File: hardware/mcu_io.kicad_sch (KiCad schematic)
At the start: 23 parts, among them J4 SWD, U10 74HC595D, U11 74HC595D, U12 74HC595D, U13 74HC595D, U6 74HC165D, U7 74HC165D, U8 74HC165D, U9 74HC165D

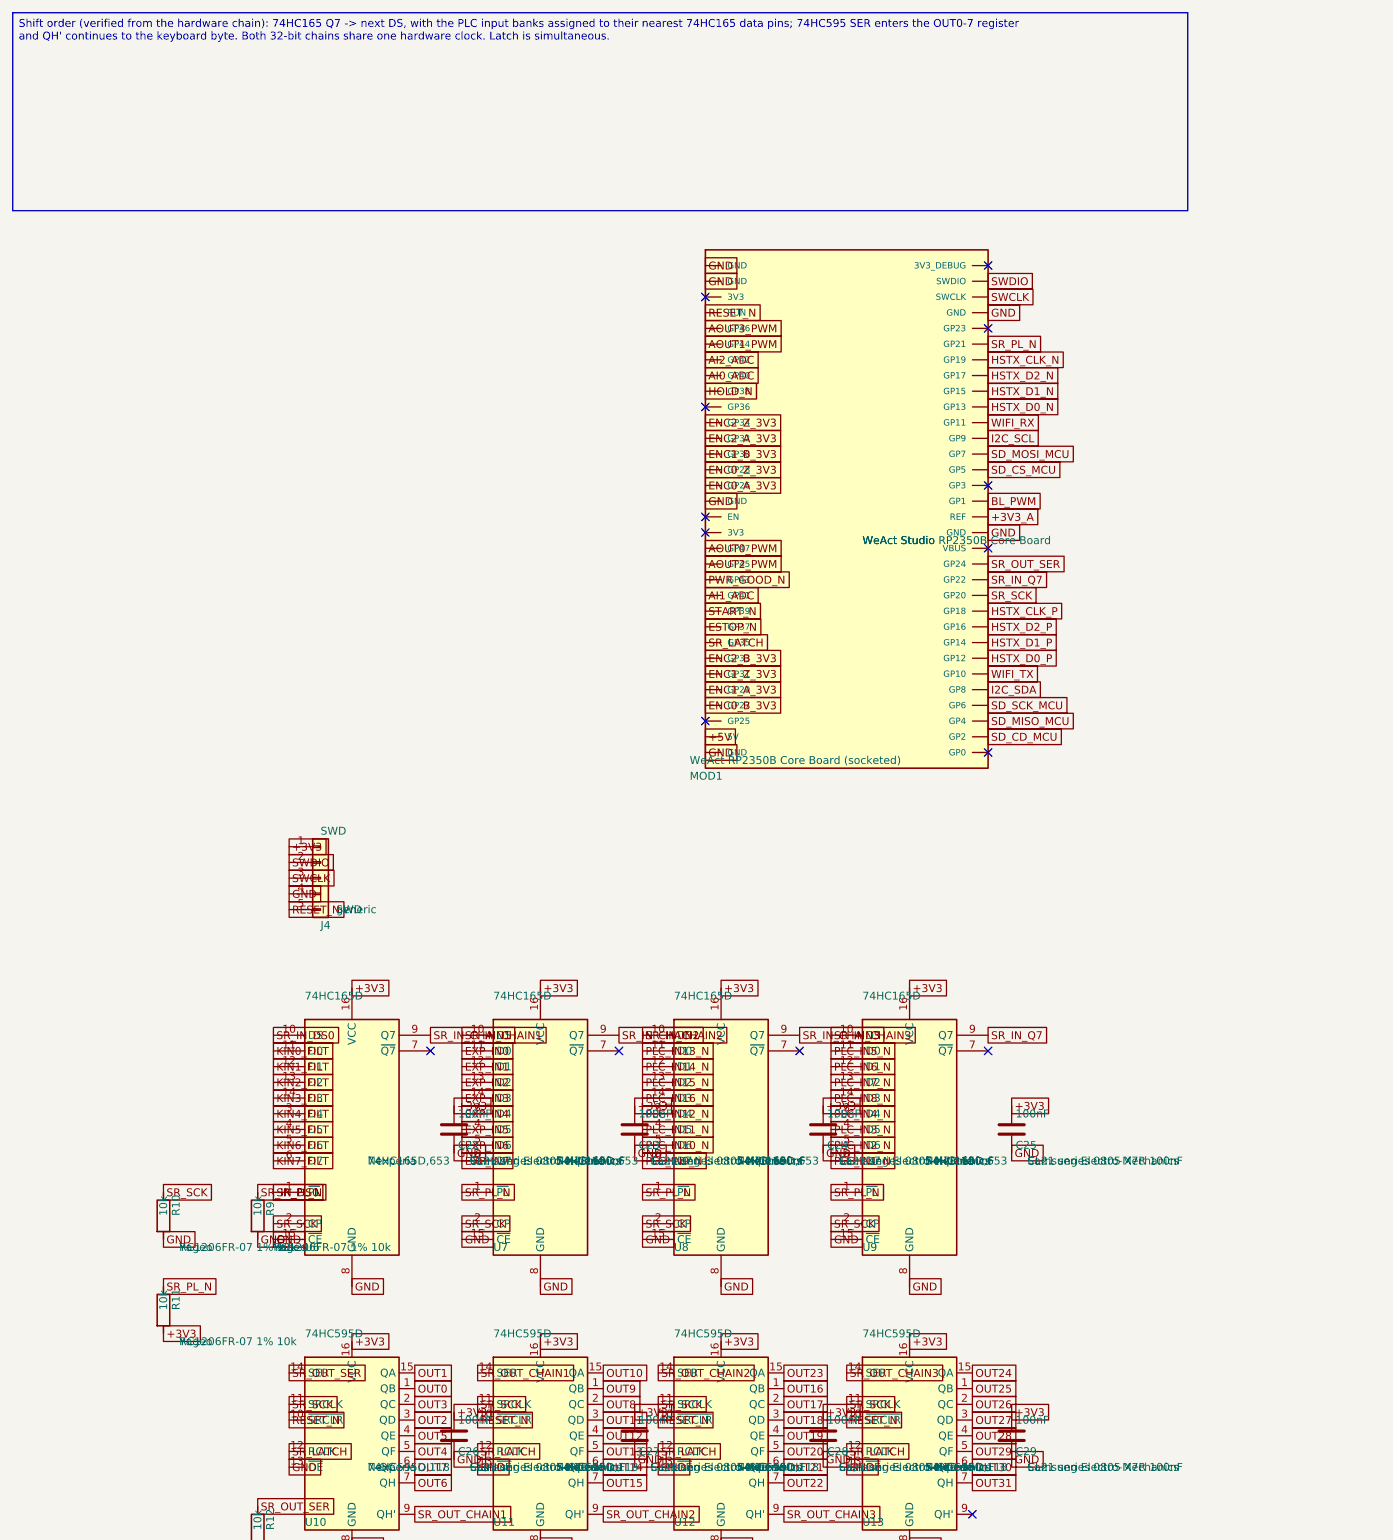
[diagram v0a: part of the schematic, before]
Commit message: Update RP2350B PCB, pinout and fabrication rules
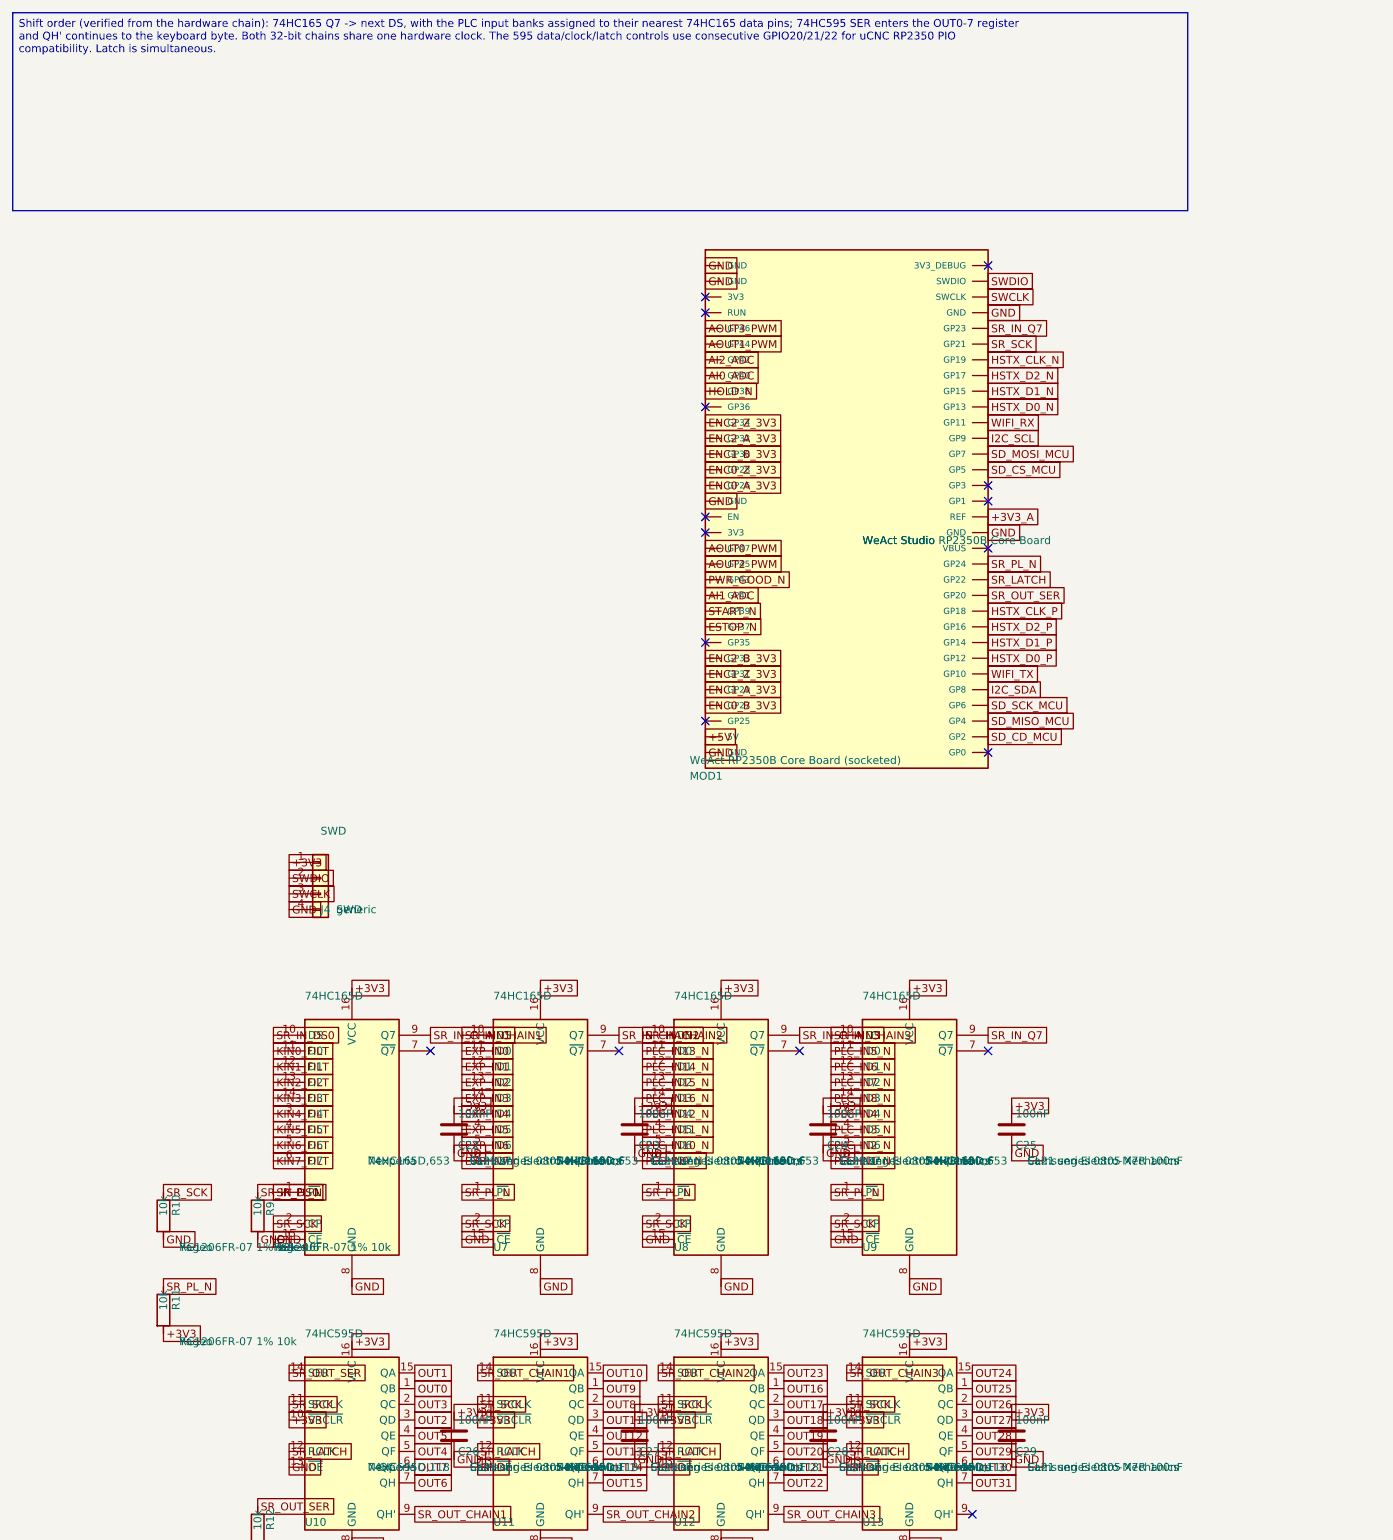
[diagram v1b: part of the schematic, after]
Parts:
- removed J4: SWD, Connector_PinHeader_2.54mm:PinHeader_1x05_P2.54mm_Vertical, symbol Connector_Generic:Conn_01x05
- added J4: SWD, Connector_PinHeader_2.54mm:PinHeader_1x04_P2.54mm_Vertical, symbol Connector_Generic:Conn_01x04
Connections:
- net +3V3: now also U10.10 (~{SRCLR}), U11.10 (~{SRCLR}), U12.10 (~{SRCLR}), U13.10 (~{SRCLR}), J4.1 (Pin_1)
- net GND: now also J4.4 (Pin_4)
- net SR_IN_Q7: now also MOD1.60 (GP23); no longer MOD1.44 (GP22)
- net SR_LATCH: now also MOD1.44 (GP22); no longer MOD1.25 (GP35)
- net SR_OUT_SER: now also MOD1.43 (GP20); no longer MOD1.45 (GP24)
- net SR_PL_N: now also MOD1.45 (GP24); no longer MOD1.59 (GP21)
- net SR_SCK: now also MOD1.59 (GP21); no longer MOD1.43 (GP20)
- net SWCLK: now also J4.3 (Pin_3)
- net SWDIO: now also J4.2 (Pin_2)
- net BL_PWM: no longer names the net of MOD1.49 (GP1)
- removed net RESET_N: MOD1.4 (RUN), U10.10 (~{SRCLR}), U11.10 (~{SRCLR}), U12.10 (~{SRCLR}), U13.10 (~{SRCLR})
- no-connect marks 15 -> 17
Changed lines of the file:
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@@
 		(instances
 			(project "MCU, shift chains and safety"
-				(path "/25c780e5-c6e9-4559-969f-d8c3f97e8b52"
+				(path "/75c4b43e-1edc-48d3-8217-1213416fdce8"
 					(reference "MOD1")
 					(unit 1)
@@
 	)
 	(symbol
-		(lib_id "Connector_Generic:Conn_01x05")
+		(lib_id "Connector_Generic:Conn_01x04")
 		(at 64.77 154.94 0)
 		(unit 1)
@@
 		(fields_autoplaced no)
 		(property "Reference" "J4"
-			(at 64.77 162.56 0.0000)
+			(at 64.77 160.02 0.0000)
 			(effects
 				(font
@@
 			)
 		)
-		(property "Footprint" "Connector_PinHeader_2.54mm:PinHeader_1x05_P2.54mm_Vertical"
+		(property "Footprint" "Connector_PinHeader_2.54mm:PinHeader_1x04_P2.54mm_Vertical"
 			(at 64.77 154.94 0.0000)
 			(effects
@@
 		(pin "4"
 		)
-		(pin "5"
-		)
 		(instances
 			(project "MCU, shift chains and safety"
-				(path "/25c780e5-c6e9-4559-969f-d8c3f97e8b52"
+				(path "/75c4b43e-1edc-48d3-8217-1213416fdce8"
 					(reference "J4")
 					(unit 1)
@@
 		(instances
 			(project "MCU, shift chains and safety"
-				(path "/25c780e5-c6e9-4559-969f-d8c3f97e8b52"
+				(path "/75c4b43e-1edc-48d3-8217-1213416fdce8"
 					(reference "U6")
 					(unit 1)
@@
 		(instances
 			(project "MCU, shift chains and safety"
-				(path "/25c780e5-c6e9-4559-969f-d8c3f97e8b52"
+				(path "/75c4b43e-1edc-48d3-8217-1213416fdce8"
 					(reference "C22")
 					(unit 1)
@@
 		(instances
 			(project "MCU, shift chains and safety"
-				(path "/25c780e5-c6e9-4559-969f-d8c3f97e8b52"
+				(path "/75c4b43e-1edc-48d3-8217-1213416fdce8"
 					(reference "U7")
 					(unit 1)
@@
 		(instances
 			(project "MCU, shift chains and safety"
-				(path "/25c780e5-c6e9-4559-969f-d8c3f97e8b52"
+				(path "/75c4b43e-1edc-48d3-8217-1213416fdce8"
 					(reference "C23")
 					(unit 1)
@@
 		(instances
 			(project "MCU, shift chains and safety"
-				(path "/25c780e5-c6e9-4559-969f-d8c3f97e8b52"
+				(path "/75c4b43e-1edc-48d3-8217-1213416fdce8"
 					(reference "U8")
 					(unit 1)
@@
 		(instances
 			(project "MCU, shift chains and safety"
-				(path "/25c780e5-c6e9-4559-969f-d8c3f97e8b52"
+				(path "/75c4b43e-1edc-48d3-8217-1213416fdce8"
 					(reference "C24")
 					(unit 1)
@@
 		(instances
 			(project "MCU, shift chains and safety"
-				(path "/25c780e5-c6e9-4559-969f-d8c3f97e8b52"
+				(path "/75c4b43e-1edc-48d3-8217-1213416fdce8"
 					(reference "U9")
 					(unit 1)
@@
 		(instances
 			(project "MCU, shift chains and safety"
-				(path "/25c780e5-c6e9-4559-969f-d8c3f97e8b52"
+				(path "/75c4b43e-1edc-48d3-8217-1213416fdce8"
 					(reference "C25")
 					(unit 1)
@@
 		(instances
 			(project "MCU, shift chains and safety"
-				(path "/25c780e5-c6e9-4559-969f-d8c3f97e8b52"
+				(path "/75c4b43e-1edc-48d3-8217-1213416fdce8"
 					(reference "R9")
 					(unit 1)
@@
 		(instances
 			(project "MCU, shift chains and safety"
-				(path "/25c780e5-c6e9-4559-969f-d8c3f97e8b52"
+				(path "/75c4b43e-1edc-48d3-8217-1213416fdce8"
 					(reference "R10")
 					(unit 1)
@@
 		(instances
 			(project "MCU, shift chains and safety"
-				(path "/25c780e5-c6e9-4559-969f-d8c3f97e8b52"
+				(path "/75c4b43e-1edc-48d3-8217-1213416fdce8"
 					(reference "R11")
 					(unit 1)
@@
 		(instances
 			(project "MCU, shift chains and safety"
-				(path "/25c780e5-c6e9-4559-969f-d8c3f97e8b52"
+				(path "/75c4b43e-1edc-48d3-8217-1213416fdce8"
 					(reference "U10")
 					(unit 1)
@@
 		(instances
 			(project "MCU, shift chains and safety"
-				(path "/25c780e5-c6e9-4559-969f-d8c3f97e8b52"
+				(path "/75c4b43e-1edc-48d3-8217-1213416fdce8"
 					(reference "C26")
 					(unit 1)
@@
 		(instances
 			(project "MCU, shift chains and safety"
-				(path "/25c780e5-c6e9-4559-969f-d8c3f97e8b52"
+				(path "/75c4b43e-1edc-48d3-8217-1213416fdce8"
 					(reference "U11")
 					(unit 1)
@@
 		(instances
 			(project "MCU, shift chains and safety"
-				(path "/25c780e5-c6e9-4559-969f-d8c3f97e8b52"
+				(path "/75c4b43e-1edc-48d3-8217-1213416fdce8"
 					(reference "C27")
 					(unit 1)
@@
 		(instances
 			(project "MCU, shift chains and safety"
-				(path "/25c780e5-c6e9-4559-969f-d8c3f97e8b52"
+				(path "/75c4b43e-1edc-48d3-8217-1213416fdce8"
 					(reference "U12")
 					(unit 1)
@@
 		(instances
 			(project "MCU, shift chains and safety"
-				(path "/25c780e5-c6e9-4559-969f-d8c3f97e8b52"
+				(path "/75c4b43e-1edc-48d3-8217-1213416fdce8"
 					(reference "C28")
 					(unit 1)
@@
 		(instances
 			(project "MCU, shift chains and safety"
-				(path "/25c780e5-c6e9-4559-969f-d8c3f97e8b52"
+				(path "/75c4b43e-1edc-48d3-8217-1213416fdce8"
 					(reference "U13")
 					(unit 1)
@@
 		(instances
 			(project "MCU, shift chains and safety"
-				(path "/25c780e5-c6e9-4559-969f-d8c3f97e8b52"
+				(path "/75c4b43e-1edc-48d3-8217-1213416fdce8"
 					(reference "C29")
 					(unit 1)
@@
 		(instances
 			(project "MCU, shift chains and safety"
-				(path "/25c780e5-c6e9-4559-969f-d8c3f97e8b52"
+				(path "/75c4b43e-1edc-48d3-8217-1213416fdce8"
 					(reference "R12")
 					(unit 1)
@@
 		(instances
 			(project "MCU, shift chains and safety"
-				(path "/25c780e5-c6e9-4559-969f-d8c3f97e8b52"
+				(path "/75c4b43e-1edc-48d3-8217-1213416fdce8"
 					(reference "R13")
 					(unit 1)
@@
 		)
 	)
-	(global_label "RESET_N"
-		(shape passive)
-		(at 127 63.5 0.0000)
-		(fields_autoplaced yes)
-		(effects
-			(font
-				(size 1.27 1.27)
-			)
-			(justify left bottom)
-		)
-	)
 	(global_label "AOUT3_PWM"
 		(shape passive)
@@
 		)
 	)
-	(global_label "SR_LATCH"
-		(shape passive)
-		(at 127 116.84 0.0000)
-		(fields_autoplaced yes)
-		(effects
-			(font
-				(size 1.27 1.27)
-			)
-			(justify left bottom)
-		)
-	)
 	(global_label "ENC2_B_3V3"
 		(shape passive)
@@
 		)
 	)
-	(global_label "SR_SCK"
+	(global_label "SR_OUT_SER"
 		(shape passive)
 		(at 172.72 109.22 0.0000)
@@
 		)
 	)
-	(global_label "SR_IN_Q7"
+	(global_label "SR_LATCH"
 		(shape passive)
 		(at 172.72 106.68 0.0000)
@@
 		)
 	)
-	(global_label "SR_OUT_SER"
+	(global_label "SR_PL_N"
 		(shape passive)
 		(at 172.72 104.14 0.0000)
@@
 		)
 	)
-	(global_label "BL_PWM"
-		(shape passive)
-		(at 172.72 93.98 0.0000)
-		(fields_autoplaced yes)
-		(effects
-			(font
-				(size 1.27 1.27)
-			)
-			(justify left bottom)
-		)
-	)
 	(global_label "SD_CS_MCU"
 		(shape passive)
@@
 		)
 	)
-	(global_label "SR_PL_N"
+	(global_label "SR_SCK"
 		(shape passive)
 		(at 172.72 68.58 0.0000)
@@
 		)
 	)
-	(global_label "GND"
+	(global_label "SR_IN_Q7"
 		(shape passive)
-		(at 172.72 63.5 0.0000)
+		(at 172.72 66.04 0.0000)
 		(fields_autoplaced yes)
 		(effects
@@
 		)
 	)
-	(global_label "SWCLK"
+	(global_label "GND"
 		(shape passive)
-		(at 172.72 60.96 0.0000)
+		(at 172.72 63.5 0.0000)
 		(fields_autoplaced yes)
 		(effects
@@
 		)
 	)
-	(global_label "SWDIO"
+	(global_label "SWCLK"
 		(shape passive)
-		(at 172.72 58.42 0.0000)
+		(at 172.72 60.96 0.0000)
 		(fields_autoplaced yes)
 		(effects
@@
 		)
 	)
-	(global_label "+3V3"
+	(global_label "SWDIO"
 		(shape passive)
-		(at 59.69 149.86 0.0000)
+		(at 172.72 58.42 0.0000)
 		(fields_autoplaced yes)
 		(effects
@@
 		)
 	)
-	(global_label "SWDIO"
+	(global_label "+3V3"
 		(shape passive)
 		(at 59.69 152.4 0.0000)
@@
 		)
 	)
-	(global_label "SWCLK"
+	(global_label "SWDIO"
 		(shape passive)
 		(at 59.69 154.94 0.0000)
@@
 		)
 	)
-	(global_label "GND"
+	(global_label "SWCLK"
 		(shape passive)
 		(at 59.69 157.48 0.0000)
@@
 		)
 	)
-	(global_label "RESET_N"
+	(global_label "GND"
 		(shape passive)
 		(at 59.69 160.02 0.0000)
@@
 		)
 	)
-	(global_label "RESET_N"
+	(global_label "+3V3"
 		(shape passive)
 		(at 59.69 242.57 0.0000)
@@
 		)
 	)
-	(global_label "RESET_N"
+	(global_label "+3V3"
 		(shape passive)
 		(at 90.17 242.57 0.0000)
@@
 		)
 	)
-	(global_label "RESET_N"
+	(global_label "+3V3"
 		(shape passive)
 		(at 119.38 242.57 0.0000)
@@
 		)
 	)
-	(global_label "RESET_N"
+	(global_label "+3V3"
 		(shape passive)
 		(at 149.86 242.57 0.0000)
@@
 	)
 	(no_connect
+		(at 127 63.5)
+	)
+	(no_connect
 		(at 127 78.74)
 	)
@@
 	)
 	(no_connect
+		(at 127 116.84)
+	)
+	(no_connect
 		(at 127 129.54)
 	)
@@
 	)
 	(no_connect
-		(at 172.72 91.44)
+		(at 172.72 93.98)
 	)
 	(no_connect
-		(at 172.72 66.04)
+		(at 172.72 91.44)
 	)
 	(no_connect
@@
 		(at 170.18 257.81)
 	)
-	(text_box "Shift order (verified from the hardware chain): 74HC165 Q7 -> next DS, with the PLC input banks assigned to their nearest 74HC165 data pins; 74HC595 SER enters the OUT0-7 register and QH' continues to the keyboard byte. Both 32-bit chains share one hardware clock. Latch is simultaneous."
+	(text_box "Shift order (verified from the hardware chain): 74HC165 Q7 -> next DS, with the PLC input banks assigned to their nearest 74HC165 data pins; 74HC595 SER enters the OUT0-7 register and QH' continues to the keyboard byte. Both 32-bit chains share one hardware clock. The 595 data/clock/latch controls use consecutive GPIO20/21/22 for uCNC RP2350 PIO compatibility. Latch is simultaneous."
 		(exclude_from_sim no)
 		(at 15 15 0.0000)
